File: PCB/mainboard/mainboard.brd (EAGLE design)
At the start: 100 x 50 mm, 18 parts

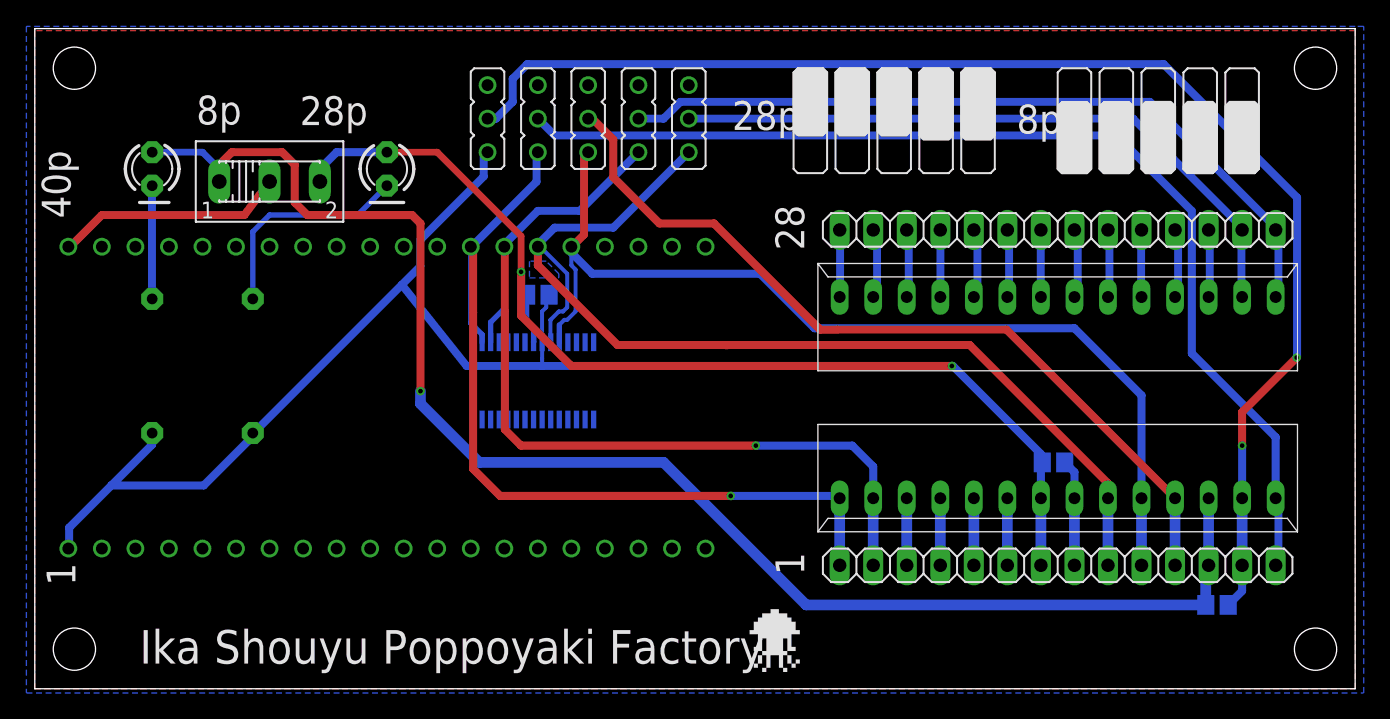
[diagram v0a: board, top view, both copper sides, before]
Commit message: Fix fonts and switch.
This commit will fix two issue.
First, use the vector font because the true type is different from prited.
Second, replace the slide switch because we used the wrong one.
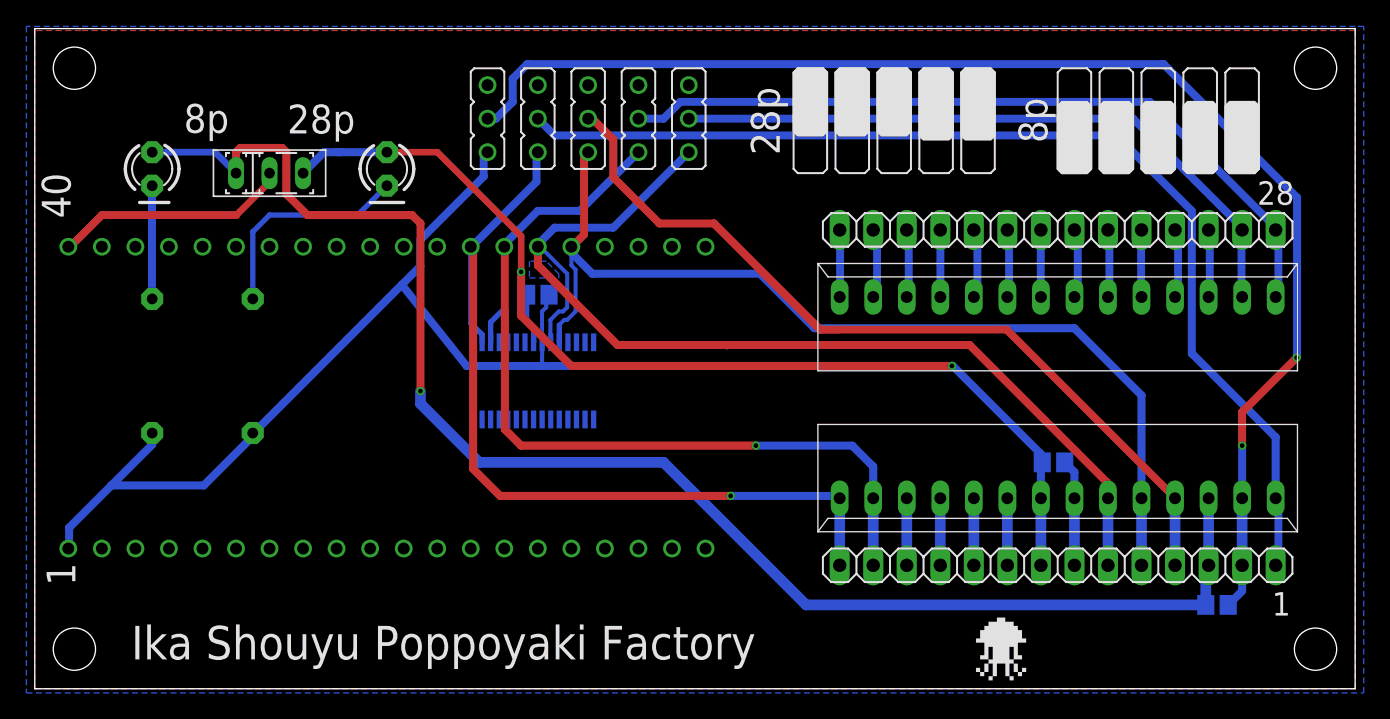
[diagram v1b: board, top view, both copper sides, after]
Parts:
- S1: device switch:255SB -> switch:M251
- moved S1 0.64 mm to (17.8, 39.1)
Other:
- board text added: "40"
- board text removed: "40p"

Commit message: Update the slik
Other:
- board text added: "3V3"
- board text added: "GND"
- board text added: "ISP"
- board text added: "RST"
- board text added: "RX"
- board text added: "TX"
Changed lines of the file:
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@@
 <?xml version="1.0" encoding="utf-8"?>
 <!DOCTYPE eagle SYSTEM "eagle.dtd">
-<eagle version="8.2.2">
+<eagle version="8.3.1">
 <drawing>
 <settings>
 <setting alwaysvectorfont="no"/>
+<setting keepoldvectorfont="yes"/>
 <setting verticaltext="up"/>
 </settings>
@@
 <vertex x="92.3925" y="44.45"/>
 </polygon>
-<text x="7.3025" y="2.2225" size="2.54" layer="21" ratio="10">Ika Shouyu Poppoyaki Factory</text>
-<text x="92.5875" y="36.655" size="1.778" layer="25">28</text>
-<text x="93.705" y="5.54" size="1.778" layer="25">1</text>
+<text x="7.3025" y="2.2225" size="2.54" layer="21" ratio="15">Ika Shouyu Poppoyaki Factory</text>
+<text x="92.5875" y="5.8575" size="1.778" layer="25">28</text>
+<text x="93.705" y="36.9725" size="1.778" layer="25">1</text>
 <text x="3.0775" y="7.815" size="2.1844" layer="25" rot="R90">1</text>
 <text x="2.7125" y="35.6325" size="2.1844" layer="25" rot="R90">40</text>
@@
 <rectangle x1="-0.16001875" y1="4.28625" x2="1.74751875" y2="4.60375" layer="200"/>
 <rectangle x1="2.38251875" y1="4.28625" x2="4.28751875" y2="4.60375" layer="200"/>
-<rectangle x1="72.23251875" y1="0.635" x2="72.55001875" y2="0.9525" layer="21"/>
-<rectangle x1="73.82001875" y1="0.635" x2="74.13751875" y2="0.9525" layer="21"/>
-<rectangle x1="71.59751875" y1="0.9525" x2="71.91248125" y2="1.27" layer="21"/>
-<rectangle x1="72.55001875" y1="0.9525" x2="72.86751875" y2="1.27" layer="21"/>
-<rectangle x1="73.50251875" y1="0.9525" x2="73.82001875" y2="1.27" layer="21"/>
-<rectangle x1="74.45501875" y1="0.9525" x2="74.77251875" y2="1.27" layer="21"/>
-<rectangle x1="71.28001875" y1="1.27" x2="71.59751875" y2="1.5875" layer="21"/>
-<rectangle x1="71.91248125" y1="1.27" x2="72.23251875" y2="1.5875" layer="21"/>
-<rectangle x1="72.55001875" y1="1.27" x2="72.86751875" y2="1.5875" layer="21"/>
-<rectangle x1="73.50251875" y1="1.27" x2="73.82001875" y2="1.5875" layer="21"/>
-<rectangle x1="74.13751875" y1="1.27" x2="74.45501875" y2="1.5875" layer="21"/>
-<rectangle x1="74.77251875" y1="1.27" x2="75.08748125" y2="1.5875" layer="21"/>
-<rectangle x1="71.91248125" y1="1.5875" x2="72.23251875" y2="1.905" layer="21"/>
-<rectangle x1="72.55001875" y1="1.5875" x2="72.86751875" y2="1.905" layer="21"/>
-<rectangle x1="73.50251875" y1="1.5875" x2="73.82001875" y2="1.905" layer="21"/>
-<rectangle x1="74.13751875" y1="1.5875" x2="74.45501875" y2="1.905" layer="21"/>
-<rectangle x1="72.23251875" y1="1.905" x2="74.13751875" y2="2.2225" layer="21"/>
-<rectangle x1="71.59751875" y1="2.2225" x2="72.23251875" y2="2.54" layer="21"/>
-<rectangle x1="72.55001875" y1="2.2225" x2="73.82001875" y2="2.54" layer="21"/>
-<rectangle x1="74.13751875" y1="2.2225" x2="74.77251875" y2="2.54" layer="21"/>
-<rectangle x1="71.91248125" y1="2.54" x2="72.23251875" y2="2.8575" layer="21"/>
-<rectangle x1="72.55001875" y1="2.54" x2="73.82001875" y2="2.8575" layer="21"/>
-<rectangle x1="74.13751875" y1="2.54" x2="74.45501875" y2="2.8575" layer="21"/>
-<rectangle x1="71.91248125" y1="2.8575" x2="72.23251875" y2="3.175" layer="21"/>
-<rectangle x1="72.55001875" y1="2.8575" x2="73.82001875" y2="3.175" layer="21"/>
-<rectangle x1="74.13751875" y1="2.8575" x2="74.45501875" y2="3.175" layer="21"/>
-<rectangle x1="71.91248125" y1="3.175" x2="74.45501875" y2="3.4925" layer="21"/>
-<rectangle x1="71.28001875" y1="3.4925" x2="75.08748125" y2="3.81" layer="21"/>
-<rectangle x1="71.59751875" y1="3.81" x2="74.77251875" y2="4.1275" layer="21"/>
-<rectangle x1="71.59751875" y1="4.1275" x2="74.77251875" y2="4.445" layer="21"/>
-<rectangle x1="71.91248125" y1="4.445" x2="74.45501875" y2="4.7625" layer="21"/>
-<rectangle x1="72.23251875" y1="4.7625" x2="74.13751875" y2="5.08" layer="21"/>
-<rectangle x1="72.86751875" y1="5.08" x2="73.50251875" y2="5.3975" layer="21"/>
+<rectangle x1="71.59751875" y1="1.27" x2="71.91501875" y2="1.5875" layer="21"/>
+<rectangle x1="73.18501875" y1="1.27" x2="73.50251875" y2="1.5875" layer="21"/>
+<rectangle x1="70.96251875" y1="1.5875" x2="71.27748125" y2="1.905" layer="21"/>
+<rectangle x1="71.91501875" y1="1.5875" x2="72.23251875" y2="1.905" layer="21"/>
+<rectangle x1="72.86751875" y1="1.5875" x2="73.18501875" y2="1.905" layer="21"/>
+<rectangle x1="73.82001875" y1="1.5875" x2="74.13751875" y2="1.905" layer="21"/>
+<rectangle x1="70.64501875" y1="1.905" x2="70.96251875" y2="2.2225" layer="21"/>
+<rectangle x1="71.27748125" y1="1.905" x2="71.59751875" y2="2.2225" layer="21"/>
+<rectangle x1="71.91501875" y1="1.905" x2="72.23251875" y2="2.2225" layer="21"/>
+<rectangle x1="72.86751875" y1="1.905" x2="73.18501875" y2="2.2225" layer="21"/>
+<rectangle x1="73.50251875" y1="1.905" x2="73.82001875" y2="2.2225" layer="21"/>
+<rectangle x1="74.13751875" y1="1.905" x2="74.45248125" y2="2.2225" layer="21"/>
+<rectangle x1="71.27748125" y1="2.2225" x2="71.59751875" y2="2.54" layer="21"/>
+<rectangle x1="71.91501875" y1="2.2225" x2="72.23251875" y2="2.54" layer="21"/>
+<rectangle x1="72.86751875" y1="2.2225" x2="73.18501875" y2="2.54" layer="21"/>
+<rectangle x1="73.50251875" y1="2.2225" x2="73.82001875" y2="2.54" layer="21"/>
+<rectangle x1="71.59751875" y1="2.54" x2="73.50251875" y2="2.8575" layer="21"/>
+<rectangle x1="70.96251875" y1="2.8575" x2="71.59751875" y2="3.175" layer="21"/>
+<rectangle x1="71.91501875" y1="2.8575" x2="73.18501875" y2="3.175" layer="21"/>
+<rectangle x1="73.50251875" y1="2.8575" x2="74.13751875" y2="3.175" layer="21"/>
+<rectangle x1="71.27748125" y1="3.175" x2="71.59751875" y2="3.4925" layer="21"/>
+<rectangle x1="71.91501875" y1="3.175" x2="73.18501875" y2="3.4925" layer="21"/>
+<rectangle x1="73.50251875" y1="3.175" x2="73.82001875" y2="3.4925" layer="21"/>
+<rectangle x1="71.27748125" y1="3.4925" x2="71.59751875" y2="3.81" layer="21"/>
+<rectangle x1="71.91501875" y1="3.4925" x2="73.18501875" y2="3.81" layer="21"/>
+<rectangle x1="73.50251875" y1="3.4925" x2="73.82001875" y2="3.81" layer="21"/>
+<rectangle x1="71.27748125" y1="3.81" x2="73.82001875" y2="4.1275" layer="21"/>
+<rectangle x1="70.64501875" y1="4.1275" x2="74.45248125" y2="4.445" layer="21"/>
+<rectangle x1="70.96251875" y1="4.445" x2="74.13751875" y2="4.7625" layer="21"/>
+<rectangle x1="70.96251875" y1="4.7625" x2="74.13751875" y2="5.08" layer="21"/>
+<rectangle x1="71.27748125" y1="5.08" x2="73.82001875" y2="5.3975" layer="21"/>
+<rectangle x1="71.59751875" y1="5.3975" x2="73.50251875" y2="5.715" layer="21"/>
+<rectangle x1="72.23251875" y1="5.715" x2="72.86751875" y2="6.0325" layer="21"/>
+<text x="61.4525" y="5.5925" size="1.27" layer="25" rot="R90">TX</text>
+<text x="63.9925" y="5.5925" size="1.27" layer="25" rot="R90">RX</text>
+<text x="76.9575" y="4.3025" size="1.27" layer="25" rot="R90">3V3</text>
+<text x="79.2325" y="4.3225" size="1.27" layer="25" rot="R90">GND</text>
+<text x="81.7725" y="4.3225" size="1.27" layer="25" rot="R90">RST</text>
+<text x="84.3125" y="4.3225" size="1.27" layer="25" rot="R90">ISP</text>
 </plain>
 <attributes>
@@
 <contactref element="MBED" pad="VOUT"/>
 <wire x1="5.08" y1="35.8775" x2="2.8" y2="33.6" width="0.6" layer="1"/>
-<wire x1="15.27775" y1="35.8775" x2="15.875" y2="35.8775" width="0" layer="19" extent="1-16"/>
 <wire x1="15.27775" y1="35.8775" x2="5.08" y2="35.8775" width="0.6" layer="1"/>
 <wire x1="2.8" y1="33.6" x2="2.54" y2="33.48" width="0.6" layer="1"/>
@@
 <compatibility>
 <note version="8.2" severity="warning">
-Since Version 8.2, Eagle supports online libraries. The ids
+Since Version 8.2, EAGLE supports online libraries. The ids
 of those online libraries will not be understood (or retained)
 with this version.

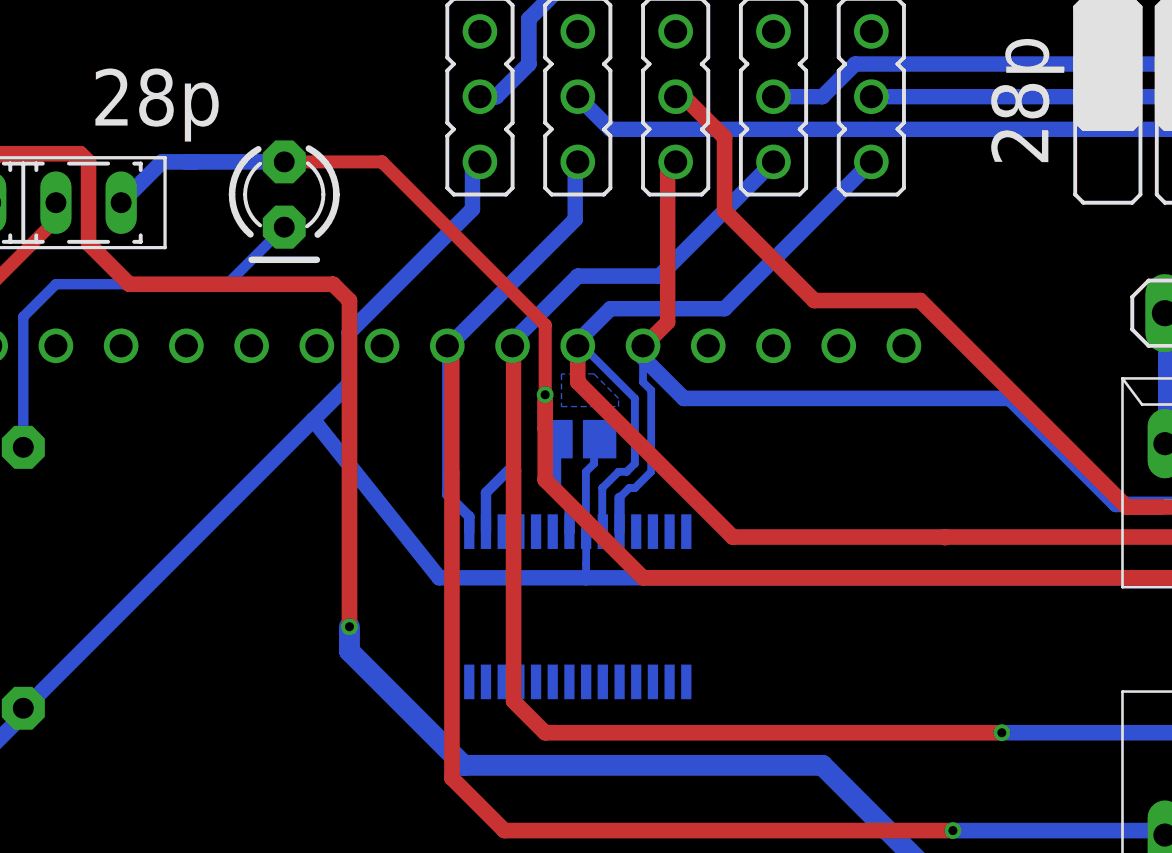
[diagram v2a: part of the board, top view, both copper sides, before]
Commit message: Fix the position of lpc1114fhd28.
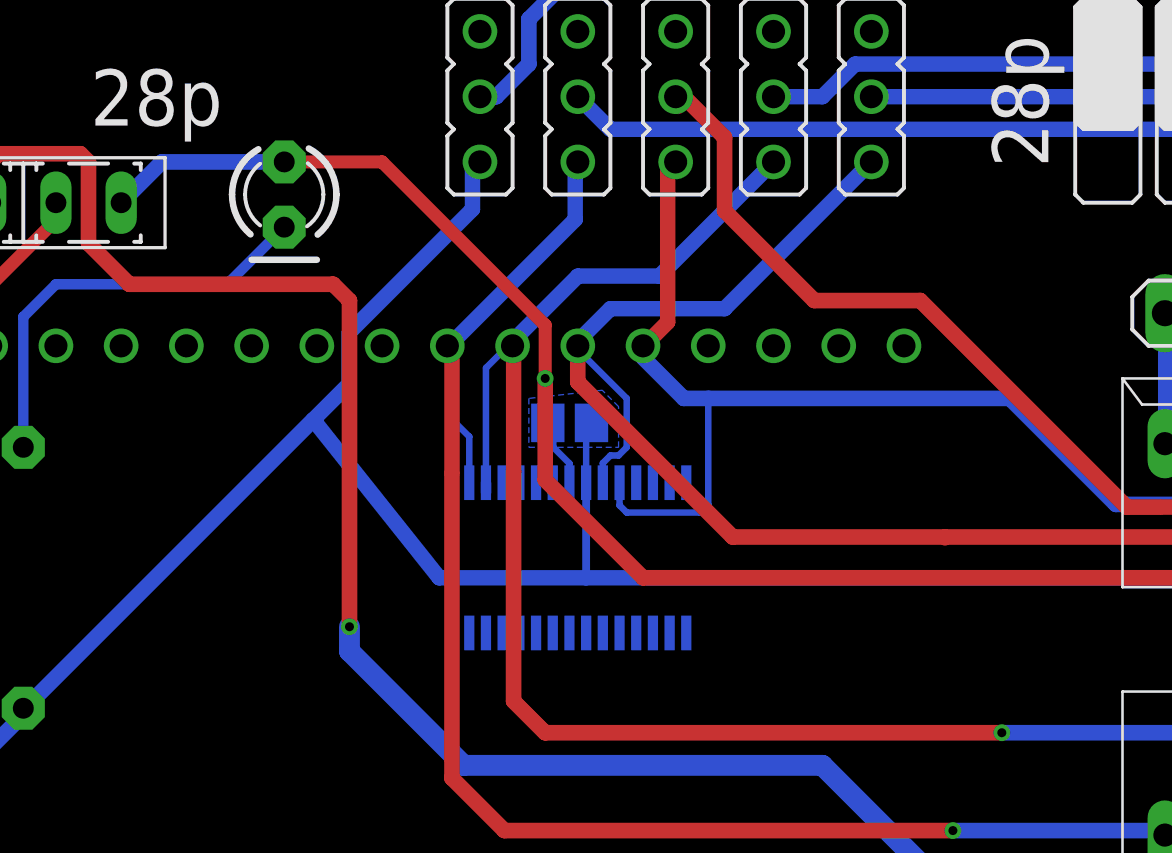
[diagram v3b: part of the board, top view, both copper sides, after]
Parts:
- moved LPC1114 1.91 mm to (38.1, 25.2)
- moved C1 0.71 mm to (37.8, 30.5)
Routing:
- net BUS4: track 81.5 -> 79.2 mm
- net BUS2: track 67.6 -> 65.7 mm
- net BUS0: track 84.1 -> 82.5 mm
- net BUS3: track 71.3 -> 69.9 mm
- net BUS5: track 77.9 -> 78.6 mm

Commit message: Update to version2.0
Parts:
- removed JP1, JP2, JP3, JP4, JP5: (no value), jumper:JP2
- removed R2: (no value), rcl:0207/10
- added S2: (no value), switch-dil:DIP05YL
- flipped R1 to the top
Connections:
- removed net N$21: LED_8P.K, R2.2
- net BUS2: now also S2.2; no longer JP2.3
- net BUS3: now also S2.5; no longer JP3.3
- net BUS4: now also S2.4; no longer JP4.3
- net BUS5: now also S2.3; no longer JP5.3
- net BUS8P1: now also S2.10; no longer JP1.2
- net BUS8P2: now also S2.9; no longer JP2.2
- net BUS8P3: now also S2.6; no longer JP3.2
- net BUS8P4: now also S2.7; no longer JP4.2
- net BUS8P5: now also S2.8; no longer JP5.2
- net GND: now also S2.1; no longer JP1.3, R2.1
- net N$2: now also LED_8P.K
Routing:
- net N$2: track 16.7 -> 26.1 mm
- net GND: track 111.1 -> 120.1 mm
- net N$21: track 8.82 -> 0.00 mm
- net BUS8P4: track 50.6 -> 57.6 mm
- net BUS4: track 79.2 -> 73.8 mm, vias 0 -> 1
- net BUS8P1: track 101.2 -> 97.4 mm
- net BUS5: track 78.6 -> 76.3 mm
- net BUS8P5: track 63.5 -> 64.7 mm
- net BUS8P3: track 58.2 -> 57.1 mm
- net BUS3: track 69.9 -> 70.7 mm
- net BUS8P2: track 83.5 -> 84.1 mm
- net BUS2: track 65.7 -> 65.0 mm
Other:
- board text added: "28p: ALL OFF"
- board text added: "8p: ALL ON"
- board text added: "OFF"
- board text added: "ON"
- board text added: "v2.0"
